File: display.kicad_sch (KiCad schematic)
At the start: 72 parts, among them IC11 SN74LV1T125DBVR, IC18 TPD8S009DSMR, IC2 TPD8S009DSMR, IC6 PCA9517ADP, J1 HDMI-Micro-D_Molex_467561001, J15 Bus_DDR4_SODIMM_CUSTOM_Jetson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, J2 DisplayPort-Mini_TE_2129320-3, T1 BSS138PW

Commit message: [#57913] fix 2309413-1
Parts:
- C1, C2, C3, C4: footprint jetson-nano-baseboard-footprints:C_0402_1005Metric -> antmicro-footprints:C_0402_1005Metric; symbol jetson-nano-baseboard:C_4u7_0402 -> antmicroCapacitors0402:C_4u7_0402
- C12, C26, C27, C39, C40, C42, C43, C44, C45, C5, C6, C7, C73, C74, C75, C76, C77, C78, C79, C8, C80: footprint jetson-nano-baseboard-footprints:C_0402_1005Metric -> antmicro-footprints:C_0402_1005Metric; symbol jetson-nano-baseboard:C_100n_0402 -> antmicroCapacitors0402:C_100n_0402
- D10, D11, D12: footprint jetson-nano-baseboard-footprints:SOT-23-3 -> antmicro-footprints:SOT-23-3; symbol jetson-nano-baseboard:PESD2USB5UV-TR -> antmicroTVSDiodes:PESD2USB5UV-TR
- D2, D4: footprint jetson-nano-baseboard-footprints:D_SOD-323F -> antmicro-footprints:D_SOD-323F; symbol jetson-nano-baseboard:1N4148WS -> antmicroDiodesRectifiersSingle:1N4148WS
- IC11: footprint jetson-nano-baseboard-footprints:SOT-23-5 -> antmicro-footprints:SOT-23-5; symbol jetson-nano-baseboard:SN74LV1T125DBVR -> antmicroLogicBuffersDriversReceiversTransceivers:SN74LV1T125DBVR
- IC18, IC2: footprint jetson-nano-baseboard-footprints:R-PDSO-N15 -> antmicro-footprints:R-PDSO-N15; symbol jetson-nano-baseboard:TPD8S009DSMR -> antmicroTVSDiodes:TPD8S009DSMR
- IC6: footprint jetson-nano-baseboard-footprints:TSSOP-8_3x3mm_P0.65mm -> antmicro-footprints:TSSOP-8_3x3mm_P0.65mm; symbol jetson-nano-baseboard:PCA9517ADP -> antmicroLogicTranslatorsLevelShifters:PCA9517ADP
- J1: footprint jetson-nano-baseboard-footprints:HDMI-Micro-D_Receptacle_Molex_467651001 -> antmicro-footprints:HDMI-Micro-D_Receptacle_Molex_467651001; symbol jetson-nano-baseboard:HDMI-Micro-D_Molex_467561001 -> antmicroVideoConnectors:HDMI-Micro-D_Molex_467561001
- J15: footprint jetson-nano-baseboard-footprints:TE_2309413 -> antmicro-footprints:TE_2309413; symbol jetson-nano-baseboard:Bus_DDR4_SODIMM_CUSTOM_Jetson-Nano-H9.2mm-socket -> antmicroSoMConnectors:Bus_DDR4_SODIMM_CUSTOM_Jetson-Nano-H9.2mm-socket
- J2: footprint jetson-nano-baseboard-footprints:DisplayPort-Mini_Receptacle_TE_2129320-3 -> antmicro-footprints:DisplayPort-Mini_Receptacle_TE_2129320-3; symbol jetson-nano-baseboard:DisplayPort-Mini_TE_2129320-3 -> antmicroVideoConnectors:DisplayPort-Mini_TE_2129320-3
- L10, L8, L9: footprint jetson-nano-baseboard-footprints:FB_0603_1608Metric -> antmicro-footprints:FB_0603_1608Metric; symbol jetson-nano-baseboard:FB_120Z_3A_Murata-BLM18SG_0603 -> antmicroFerriteBeadsandChips:FB_120Z_3A_Murata-BLM18SG_0603
- R1, R10, R2, R3, R4, R7, R8, R9: footprint jetson-nano-baseboard-footprints:R_0402_1005Metric -> antmicro-footprints:R_0402_1005Metric; symbol jetson-nano-baseboard:R_5R6_0402 -> antmicroResistors0402:R_5R6_0402
- R100, R26, R30: footprint jetson-nano-baseboard-footprints:R_0402_1005Metric -> antmicro-footprints:R_0402_1005Metric; symbol jetson-nano-baseboard:R_100k_0402 -> antmicroResistors0402:R_100k_0402
- R11, R37, R5, R6, R81, R83, R88: footprint jetson-nano-baseboard-footprints:R_0402_1005Metric -> antmicro-footprints:R_0402_1005Metric; symbol jetson-nano-baseboard:R_2k_0402 -> antmicroResistors0402:R_2k_0402
- R12, R82, R98, R99: footprint jetson-nano-baseboard-footprints:R_0402_1005Metric -> antmicro-footprints:R_0402_1005Metric; symbol jetson-nano-baseboard:R_0R_0402 -> antmicroResistors0402:R_0R_0402
- R31, R32: footprint jetson-nano-baseboard-footprints:R_0402_1005Metric -> antmicro-footprints:R_0402_1005Metric; symbol jetson-nano-baseboard:R_1M_0402 -> antmicroResistors0402:R_1M_0402
- T1: footprint jetson-nano-baseboard-footprints:SC70-3 -> antmicro-footprints:SC70-3; symbol jetson-nano-baseboard:BSS138PW -> antmicroTransistorsFETsMOSFETsSingle:BSS138PW
- TP2, TP25, TP26, TP33, TP34, TP35, TP36: footprint jetson-nano-baseboard-footprints:TP_SMD_1.5mm -> antmicro-footprints:TP_SMD_1.5mm; symbol jetson-nano-baseboard:TP_1.5mm_SMD -> antmicroTestPoints:TP_1.5mm_SMD

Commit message: [#83358] Update KiCad project files
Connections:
- net DP_CEC: no longer J2.6 (CONFIG2)
- net DP_HPD_IN: no longer J2.2 (HOTPLUG)
- net DP_MODE: now also J2.2 (HPD); no longer J2.4 (CONFIG1)
- net DP_PWR: now also D2.1 (C); no longer D2.A
- net GND: no longer J2.21 (SH), J2.22 (SH), J2.23 (SH), J2.24 (SH)
- net HDMI_PWR: now also D4.1 (C); no longer D4.A
- net at C3.1, C4.1: no longer D2.K, J2.20 (DP_PWR)
- net at C1.1, C2.1, J1.19 (+5V): no longer D4.K
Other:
- moved on the sheet: J2

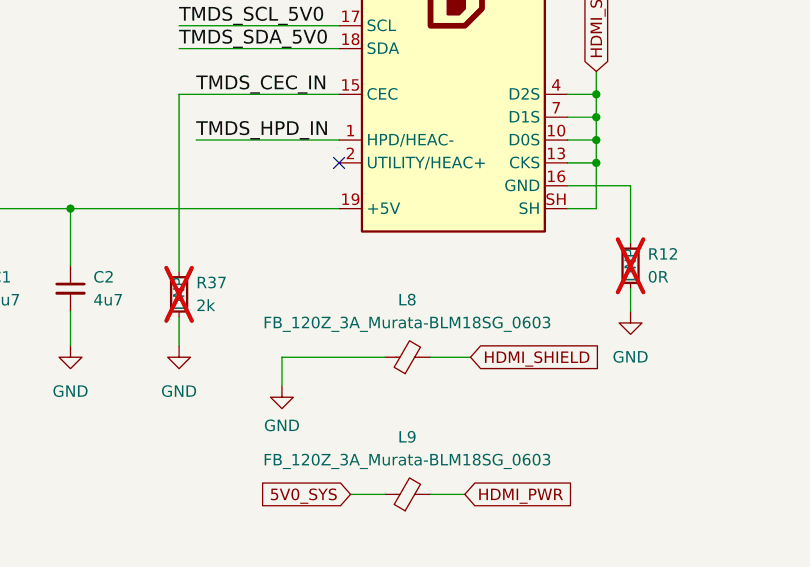
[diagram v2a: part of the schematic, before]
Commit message: [#83358] Run kmake dnp
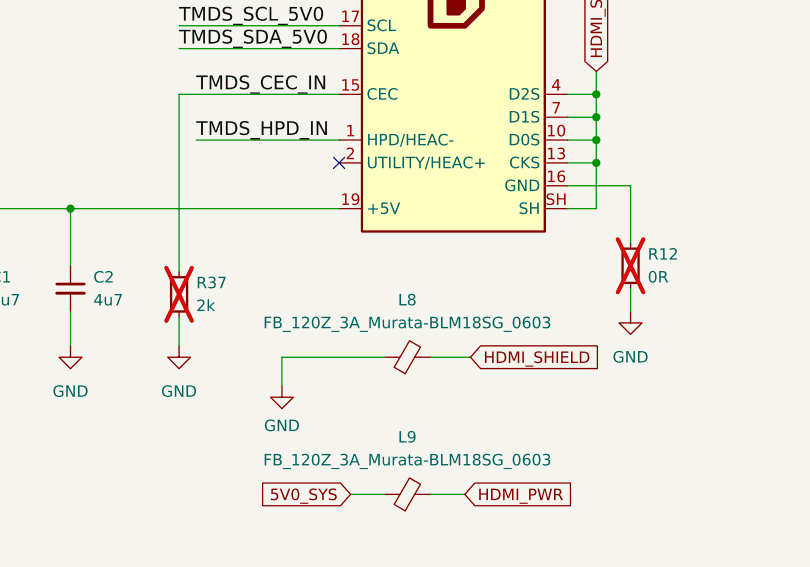
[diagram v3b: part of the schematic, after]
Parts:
- R12, R37: DNP DNP -> (none)
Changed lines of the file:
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@@
-			)
-		)
-		(property "DNP" "DNP"
-			(at 368.3 92.075 0)
-			(effects
-				(font
-					(size 1.27 1.27)
-				)
-				(justify left)
 			)
 		)
@@
 			(effects
 				(font
-					(size 1.27 1.27)
-				)
-				(justify left)
-			)
-		)
-		(property "DNP" "DNP"
-			(at 318.135 95.25 0)
-			(effects
-				(font

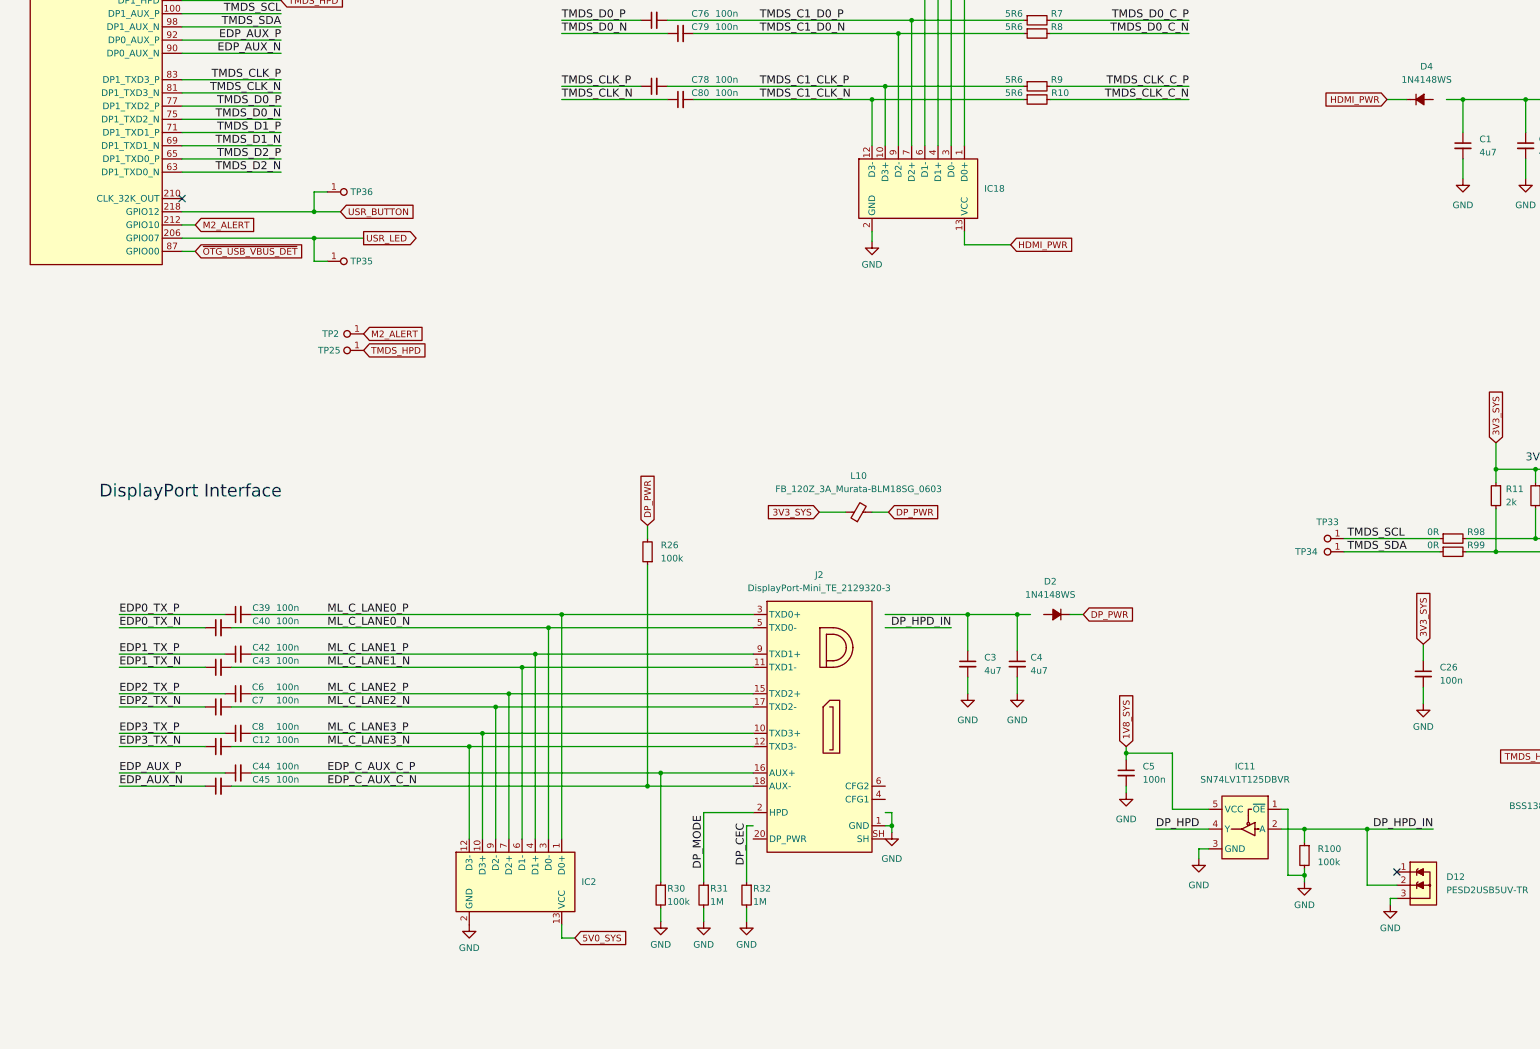
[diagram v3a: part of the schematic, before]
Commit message: [#83358] Repair broken symbol after update
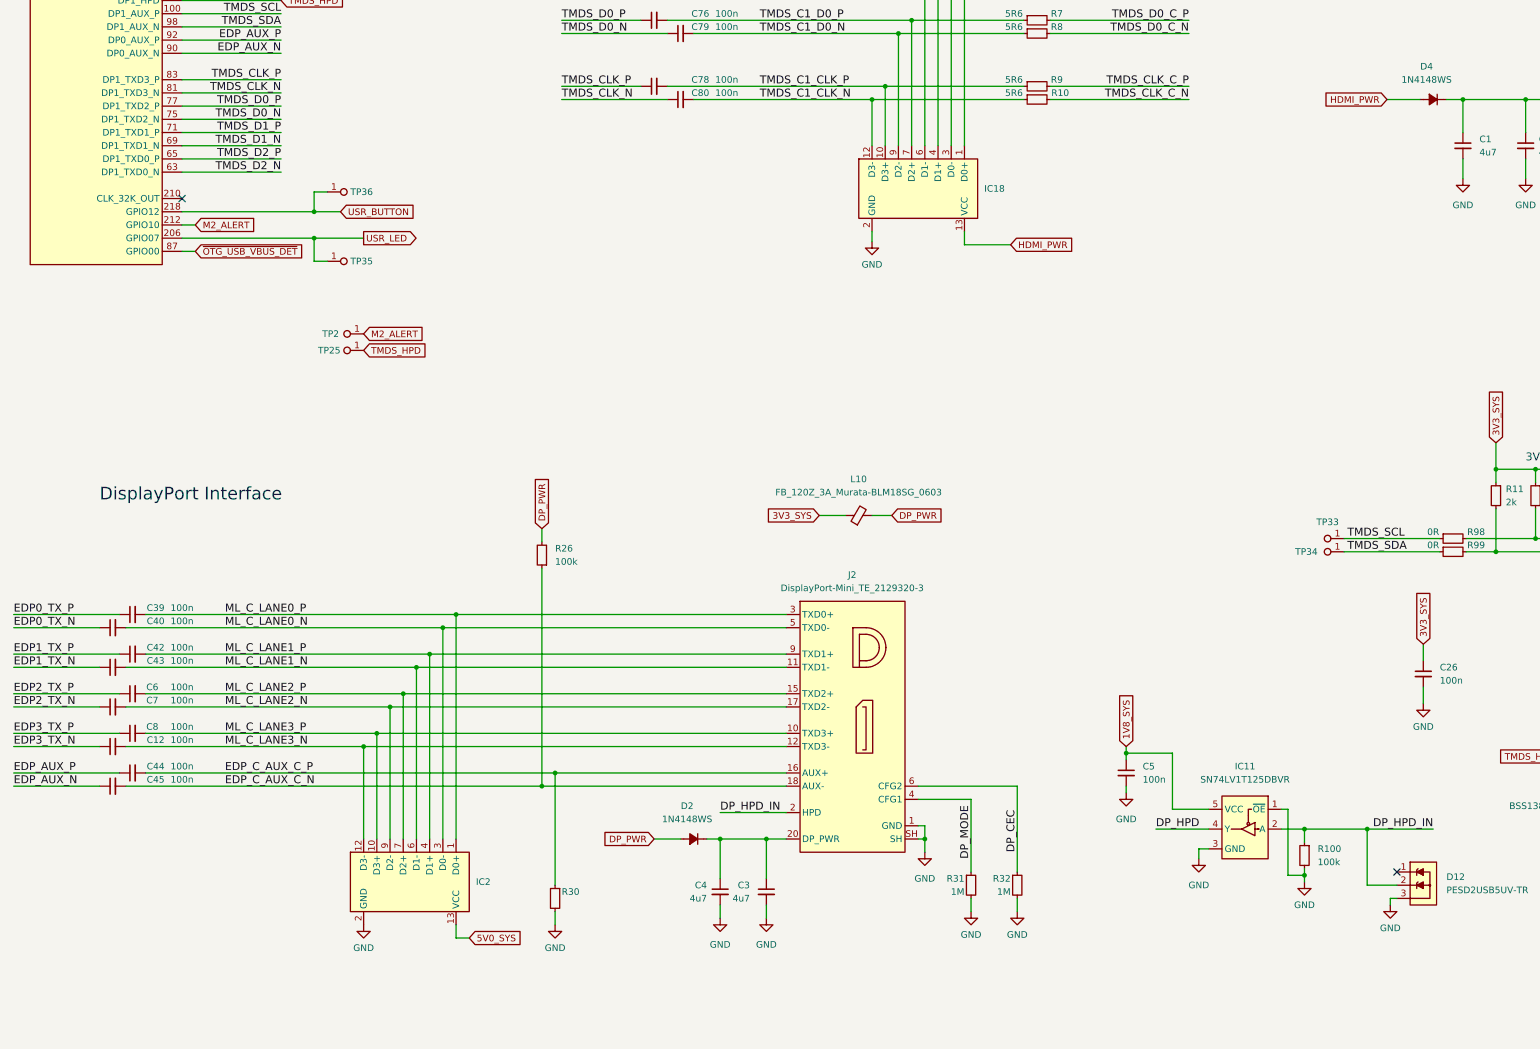
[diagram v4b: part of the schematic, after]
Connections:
- net DP_CEC: now also J2.6 (CFG2)
- net DP_HPD_IN: now also J2.2 (HPD)
- net DP_MODE: now also J2.4 (CFG1); no longer J2.2 (HPD)
- net DP_PWR: now also D2.2 (A); no longer D2.1 (C)
- net GND: now also J2.SH
- net HDMI_PWR: now also D4.2 (A); no longer D4.1 (C)
- net at C3.1, C4.1: now also D2.1 (C), J2.20 (DP_PWR)
- net at C1.1, C2.1, J1.19 (+5V): now also D4.1 (C)
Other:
- moved on the sheet: C12, C3, C39, C4, C40, C42, C43, C44, C45, C6, C7, C8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
